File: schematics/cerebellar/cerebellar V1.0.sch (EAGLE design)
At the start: 68 parts, among them CON2 ODrive1, CON4 Odrive3, CON5 ODrive4, CON6 Odrive2, CON7 ODrive5, CON8 ODrive6, IC3 LTC7001, P1 Foot1, P10 SPI2, P11 Foot2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

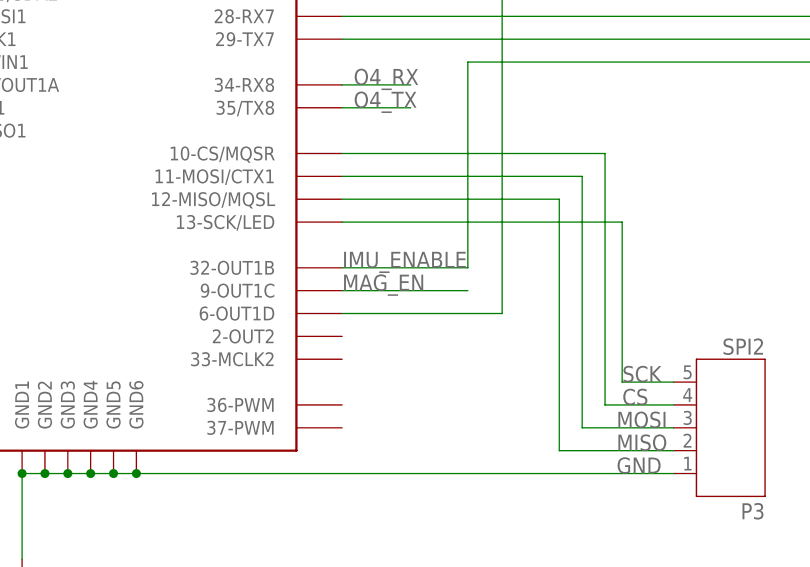
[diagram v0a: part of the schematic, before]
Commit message: buffersize in UART7 for less checksum errors
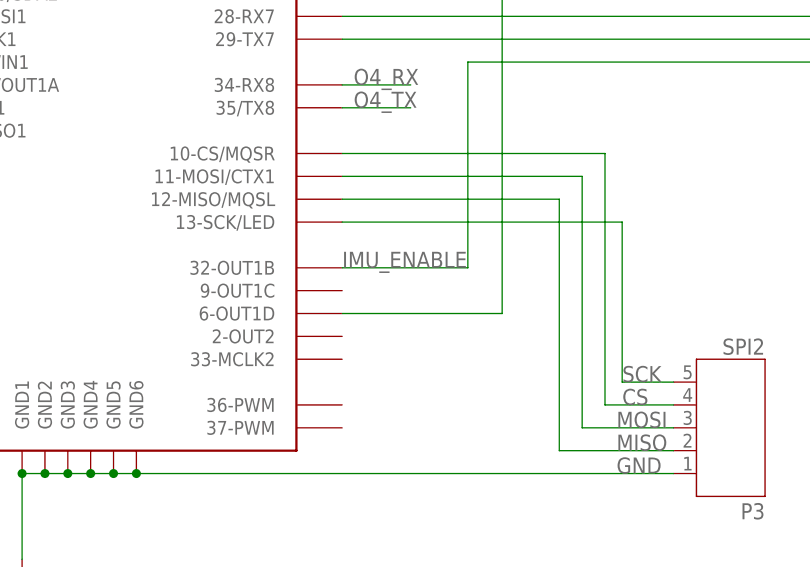
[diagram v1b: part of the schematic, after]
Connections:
- removed net MAG_EN: U$1.9-OUT1C
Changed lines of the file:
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@@
-</segment>
-</net>
-<net name="MAG_EN" class="0">
-<segment>
-<pinref part="U$1" gate="G$1" pin="9-OUT1C"/>
-<wire x1="149.86" y1="8.89" x2="163.83" y2="8.89" width="0.1524" layer="91"/>
-<label x="149.86" y="8.89" size="1.778" layer="95"/>
 </segment>
 </net>
